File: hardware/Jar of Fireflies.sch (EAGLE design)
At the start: 17 parts, among them IC1 ATTINY85, J1 POWER_JACKPTH, J3 M022.54MM_SCREWTERM

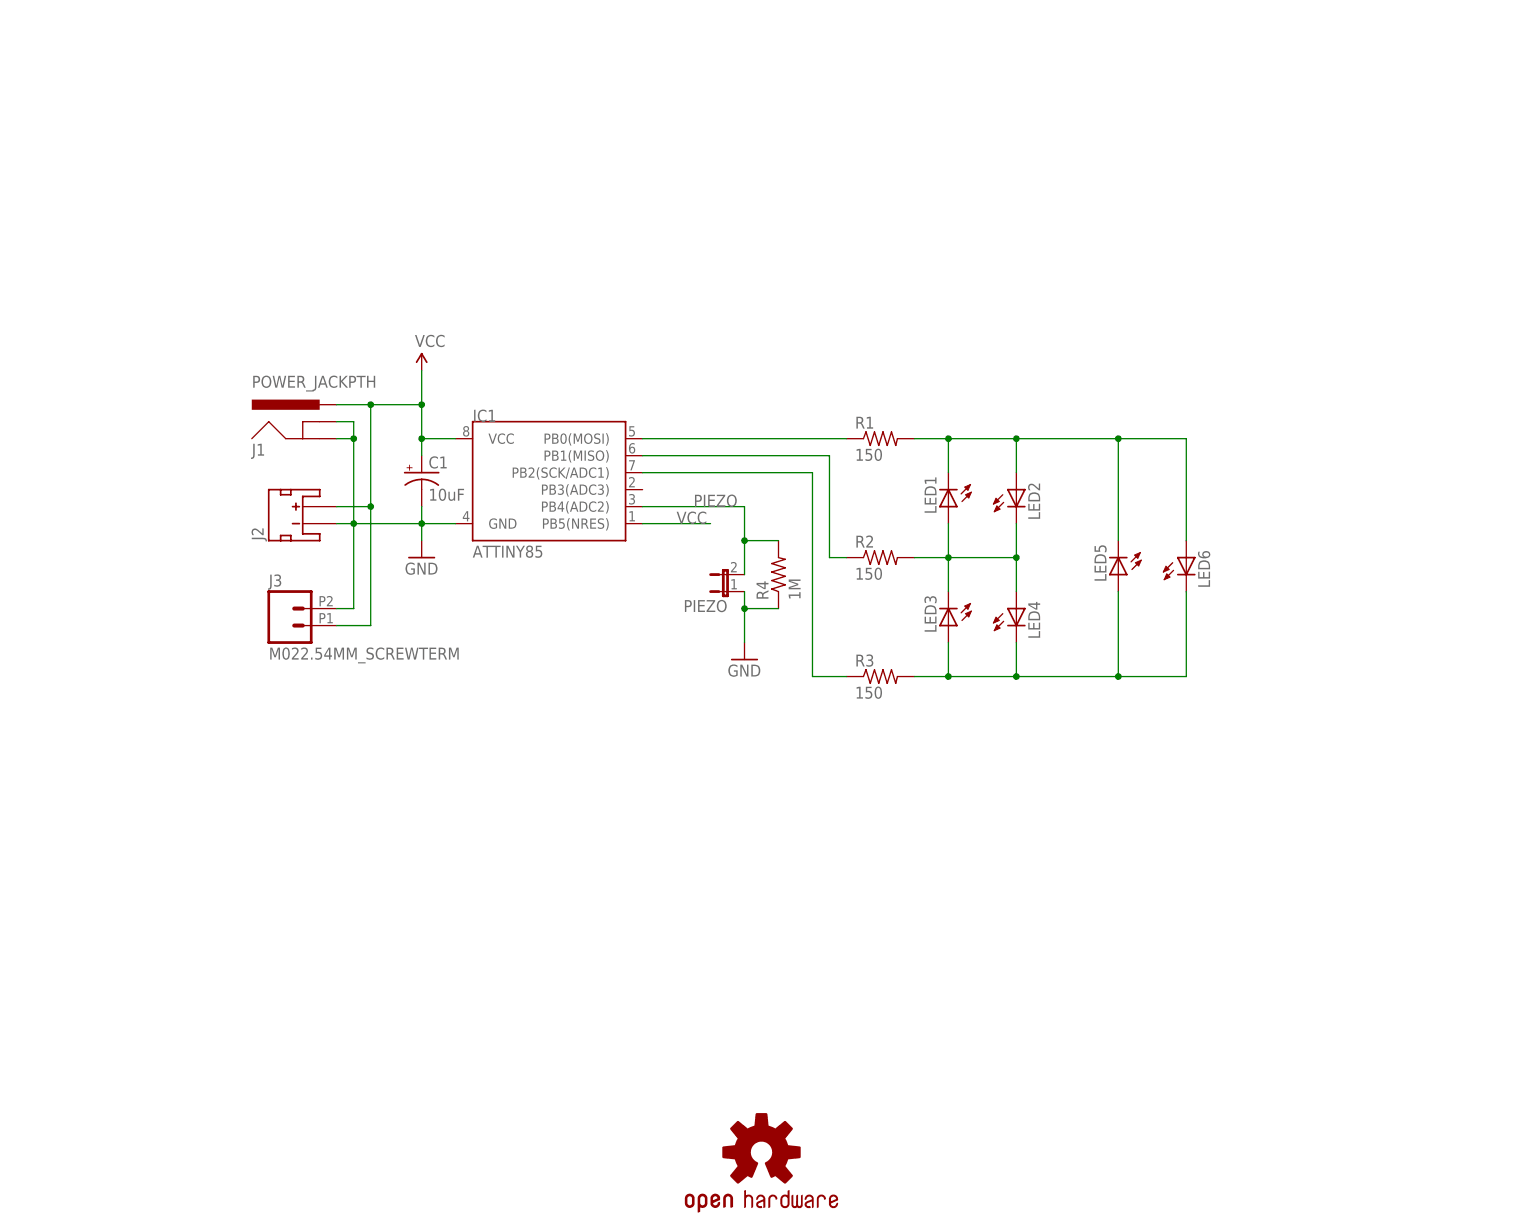
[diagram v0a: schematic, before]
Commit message: Updating PCB design with ICSP, SMD pads for LEDs, sensor interface, and different power options
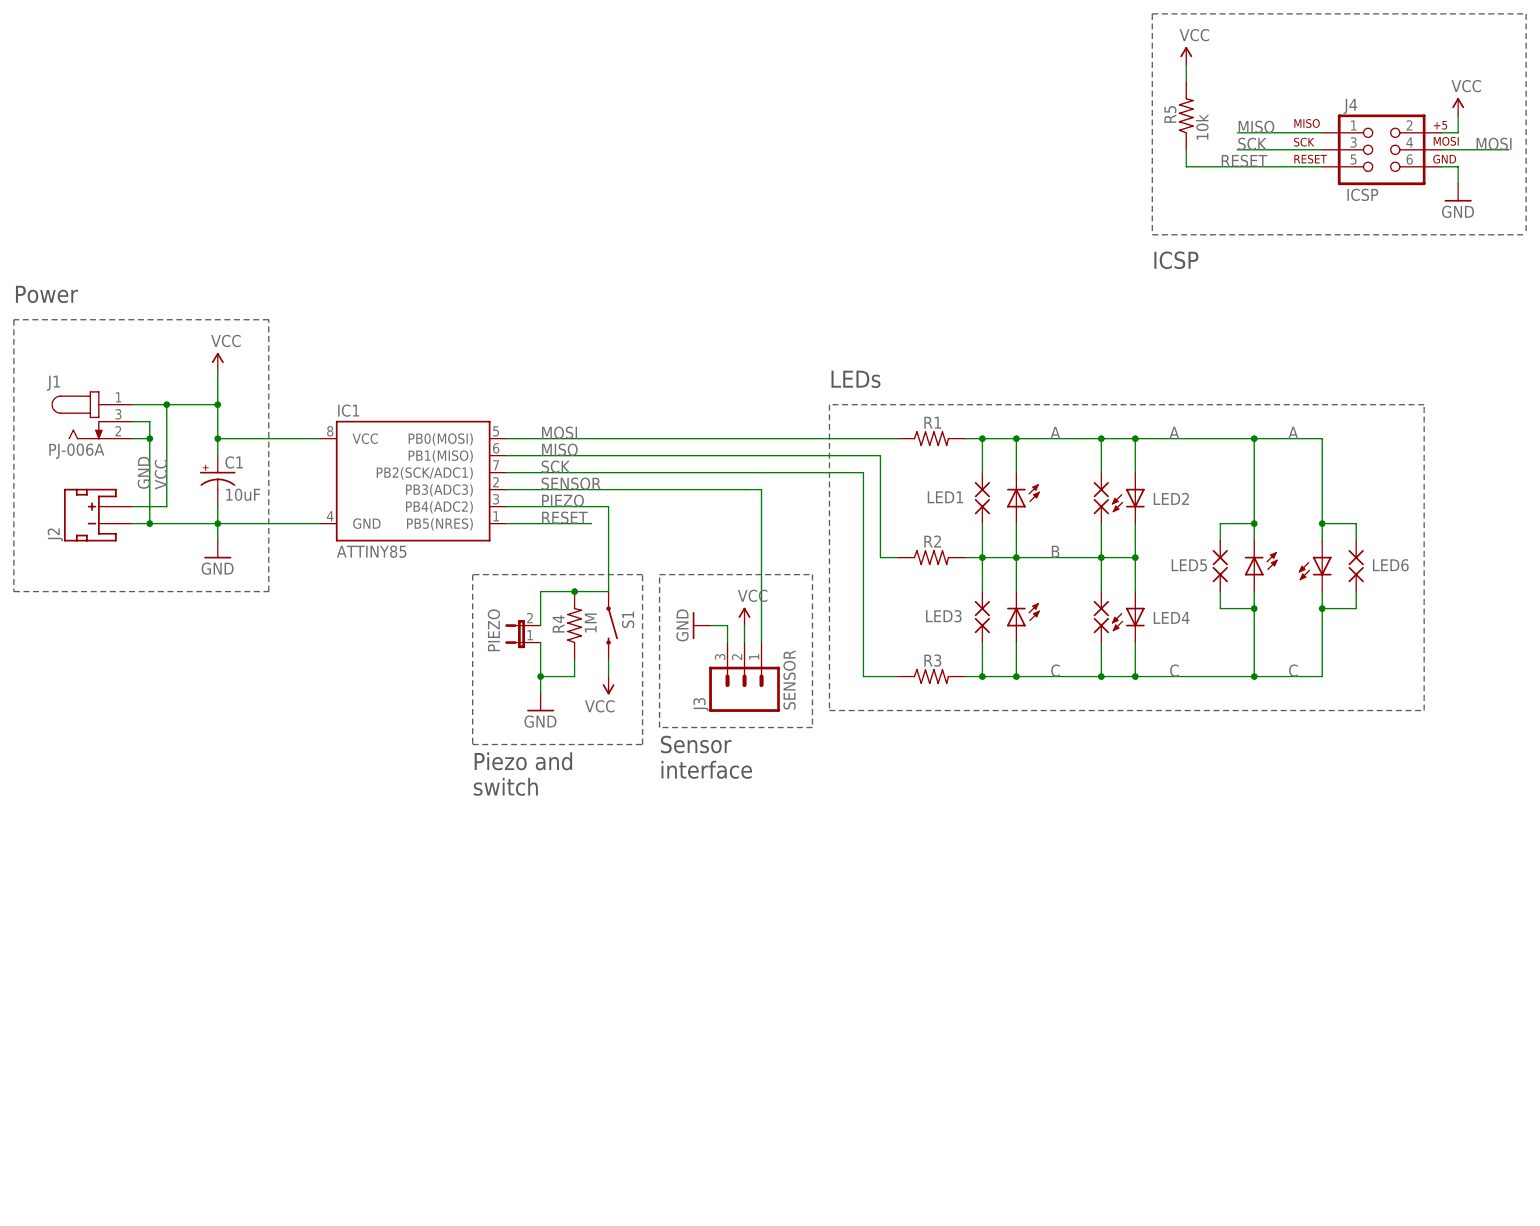
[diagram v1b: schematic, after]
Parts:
- removed LOGO1: OSHW-LOGOL, SparkFun-Aesthetics:OSHW-LOGOL
- added J4: ICSP, SparkFun-Connectors:AVR_SPI_PRG_62X3_LOCK
- added PAD1, PAD10, PAD11, PAD12, PAD2, PAD3, PAD4, PAD5, PAD6, PAD7, PAD8, PAD9: (no value), wirepad:SMD2
- added R5: 10k, resistor:R-US_0207/2V
- added S1: SWITCH-MOMENTARY-2PTH, SparkFun-Electromechanical:SWITCH-MOMENTARY-2PTH
- J1: value POWER_JACKPTH -> PJ-006A; device SparkFun-Connectors:POWER_JACKPTH -> PJ-006A:PJ-006A
- J2: value (none) -> JST
- J3: value M022.54MM_SCREWTERM -> SENSOR; device SparkFun-Connectors:M022.54MM_SCREWTERM -> SparkFun-Connectors:M03PTH
- R1, R3: value 150 -> (none)
- R2: value 150 -> (none); device resistor:R-US_0204/7 -> resistor:R-US_0207/2V
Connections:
- removed net N$1: LED1.A, LED2.C, LED3.C, LED4.A, R2.2
- removed net N$3: LED3.A, LED4.C, LED5.A, LED6.C, R3.2
- removed net PORTA: IC1.PB0(MOSI), R1.1
- removed net PORTB: IC1.PB1(MISO), R2.1
- removed net PORTC: IC1.PB2(SCK/ADC1), R3.1
- new net A: LED1.C, LED2.A, LED5.C, LED6.A, PAD1.P, PAD11.P, PAD5.P, PAD9.P, R1.2
- new net B: LED1.A, LED2.C, LED3.C, LED4.A, PAD2.P, PAD3.P, PAD6.P, PAD7.P, R2.2
- new net C: LED3.A, LED4.C, LED5.A, LED6.C, PAD10.P, PAD12.P, PAD4.P, PAD8.P, R3.2
- new net MISO: IC1.PB1(MISO), J4.1, R2.1
- new net MOSI: IC1.PB0(MOSI), J4.4, R1.1
- new net RESET: IC1.PB5(NRES), J4.5, R5.1
- new net SCK: IC1.PB2(SCK/ADC1), J4.3, R3.1
- new net SENSOR: IC1.PB3(ADC3), J3.1
- net GND: now also J1.2, J1.3, J3.3, J4.6; no longer J1.GND, J1.GNDBREAK, J3.2
- net N$2: now also PIEZO.2, R4.2, S1.1; no longer LED1.C, LED2.A, LED5.C, LED6.A, R1.2
- net PIEZO: no longer PIEZO.2, R4.2
- net VCC: now also J1.1, J3.2, J4.2, R5.2, S1.2; no longer IC1.PB5(NRES), J1.PWR, J3.1
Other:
- note added: "ICSP"
- note added: "LEDs"
- note added: "Piezo and switch"
- note added: "Power"
- note added: "Sensor interface"
- moved on the sheet: C1, IC1, J2, LED1, LED2, LED3, LED4, LED5, LED6, PIEZO, R1, R2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

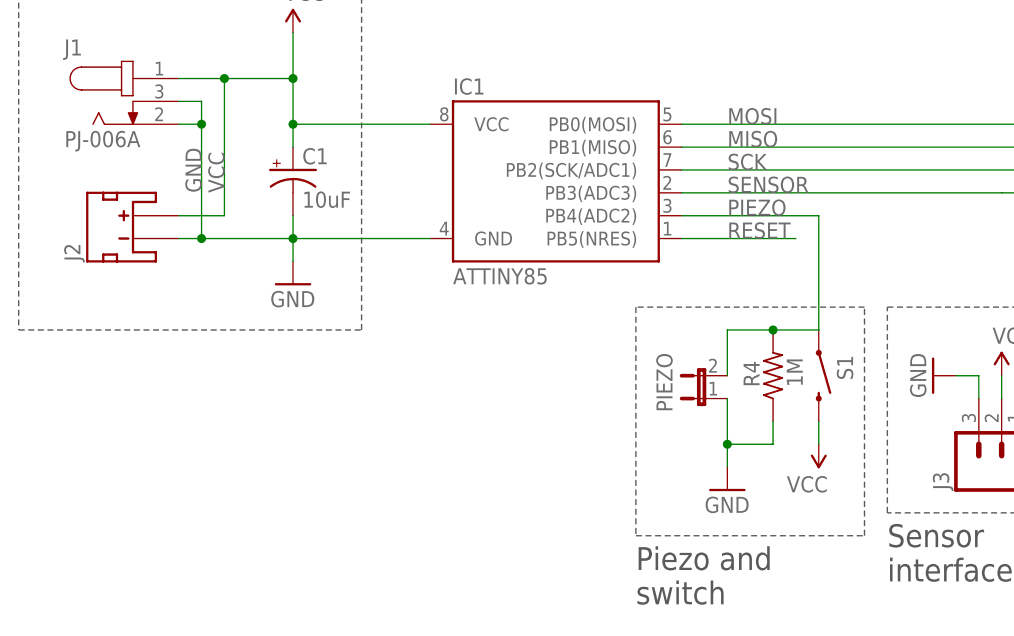
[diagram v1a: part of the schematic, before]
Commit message: Switching to vertical JST jack
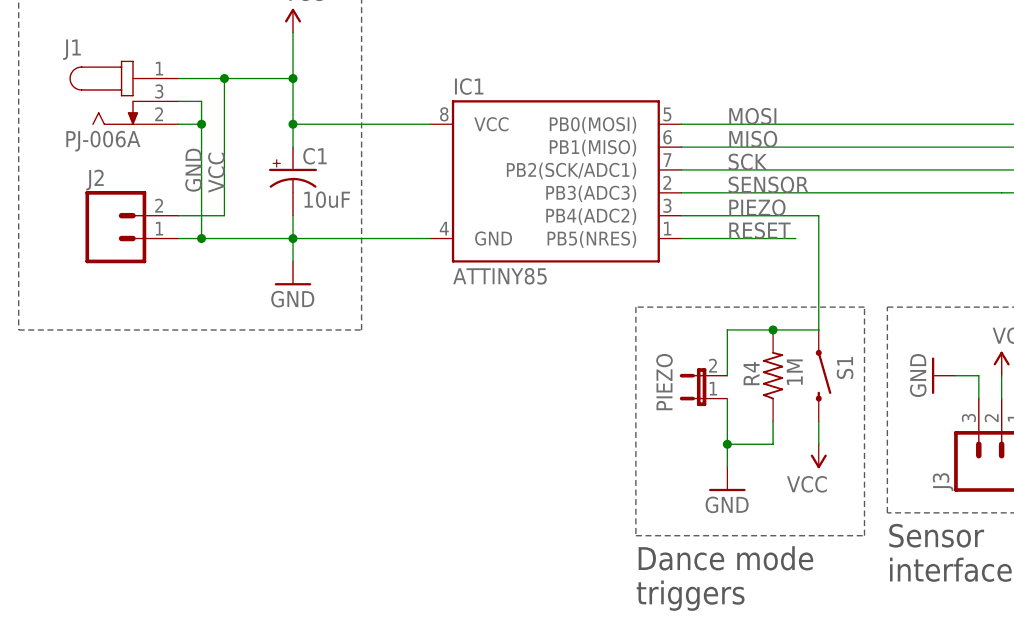
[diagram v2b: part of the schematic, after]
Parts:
- J2: value JST -> (none); device SparkFun-Connectors:JST_2MM_MALE -> SparkFun-Connectors:M02JST-PTH-VERT
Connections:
- net GND: now also J2.1; no longer J2.-
- net VCC: now also J2.2; no longer J2.+
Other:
- note added: "Dance mode triggers"
- note removed: "Piezo and switch"
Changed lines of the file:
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@@
 <part name="R3" library="resistor" deviceset="R-US_" device="0207/2V"/>
 <part name="GND2" library="supply1" deviceset="GND" device=""/>
-<part name="J2" library="SparkFun-Connectors" deviceset="JST_2MM_MALE" device="" value="JST"/>
 <part name="C1" library="SparkFun-Capacitors" deviceset="CAP_POL" device="PTH2" value="10uF"/>
 <part name="S1" library="SparkFun-Electromechanical" deviceset="SWITCH-MOMENTARY-2" device="PTH" value=""/>
@@
 <part name="GND4" library="supply1" deviceset="GND" device=""/>
 <part name="J1" library="PJ-006A" deviceset="PJ-006A" device=""/>
+<part name="J2" library="SparkFun-Connectors" deviceset="M02" device="JST-PTH-VERT"/>
 </parts>
 <sheets>
@@
 <wire x1="114.3" y1="99.06" x2="88.9" y2="99.06" width="0.1524" layer="97" style="longdash"/>
 <text x="20.32" y="139.7" size="2.54" layer="97" font="vector" ratio="15">Power</text>
-<text x="88.9" y="66.04" size="2.54" layer="97" font="vector" ratio="15">Piezo and
-switch</text>
+<text x="88.9" y="66.04" size="2.54" layer="97" font="vector" ratio="15">Dance mode
+triggers</text>
 <text x="116.84" y="68.58" size="2.54" layer="97" font="vector" ratio="15">Sensor
 interface</text>
@@
 </instance>
 <instance part="GND2" gate="1" x="99.06" y="78.74"/>
-<instance part="J2" gate="G$1" x="33.02" y="106.68" rot="R90"/>
 <instance part="C1" gate="G$1" x="50.8" y="114.3"/>
 <instance part="S1" gate="G$1" x="109.22" y="91.44" smashed="yes" rot="R270">
@@
 <instance part="GND4" gate="1" x="121.92" y="91.44" rot="R270"/>
 <instance part="J1" gate="G$1" x="33.02" y="121.92"/>
+<instance part="J2" gate="G$1" x="30.48" y="106.68"/>
 </instances>
 <busses>
@@
 <wire x1="50.8" y1="106.68" x2="50.8" y2="104.14" width="0.1524" layer="91"/>
 <pinref part="GND1" gate="1" pin="GND"/>
-<pinref part="J2" gate="G$1" pin="-"/>
 <wire x1="40.64" y1="106.68" x2="38.1" y2="106.68" width="0.1524" layer="91"/>
 <wire x1="40.64" y1="106.68" x2="40.64" y2="119.38" width="0.1524" layer="91"/>
@@
 <wire x1="40.64" y1="121.92" x2="40.64" y2="119.38" width="0.1524" layer="91"/>
 <junction x="40.64" y="119.38"/>
+<pinref part="J2" gate="G$1" pin="1"/>
 </segment>
 <segment>
@@
 <junction x="50.8" y="124.46"/>
 <wire x1="43.18" y1="124.46" x2="50.8" y2="124.46" width="0.1524" layer="91"/>
-<pinref part="J2" gate="G$1" pin="+"/>
 <wire x1="38.1" y1="109.22" x2="43.18" y2="109.22" width="0.1524" layer="91"/>
 <wire x1="43.18" y1="109.22" x2="43.18" y2="124.46" width="0.1524" layer="91"/>
@@
 <wire x1="38.1" y1="124.46" x2="43.18" y2="124.46" width="0.1524" layer="91"/>
 <junction x="43.18" y="124.46"/>
-</segment>
-<segment>
+<pinref part="J2" gate="G$1" pin="2"/>
+</segment>
+<segment>
